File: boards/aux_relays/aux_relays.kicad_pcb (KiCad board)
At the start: 2 copper layers, 82.6 x 40.1 mm, 44 parts, among them J1 Conn_01x15, J2 Conn_01x15, K1 EC2-24NU, K2 EC2-24NU, K3 EC2-24NU, K4 EC2-24NU, K5 EC2-24NU, Q1 MMBT2907, SW1 SW_SPDT, SW2 SW_SPDT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

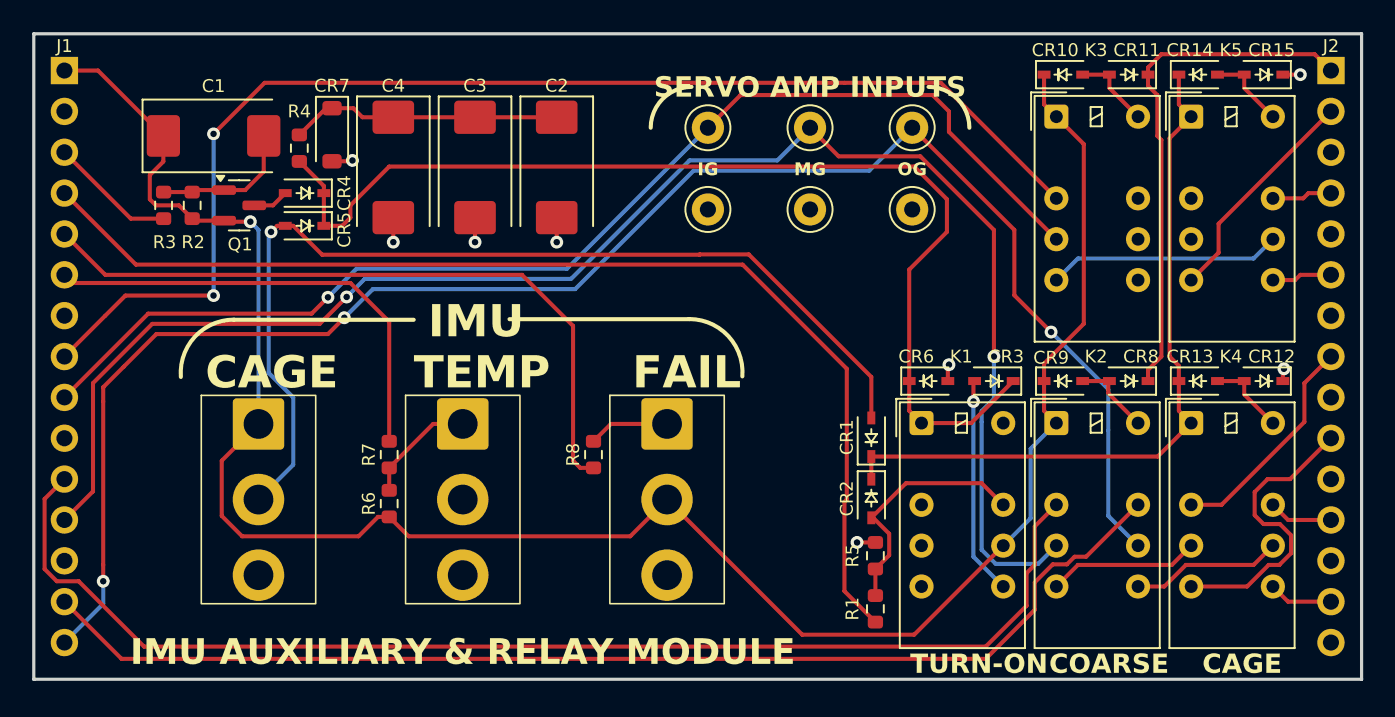
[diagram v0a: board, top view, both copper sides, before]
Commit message: Corrected switch layouts for auxiliary relays and LM switching boards
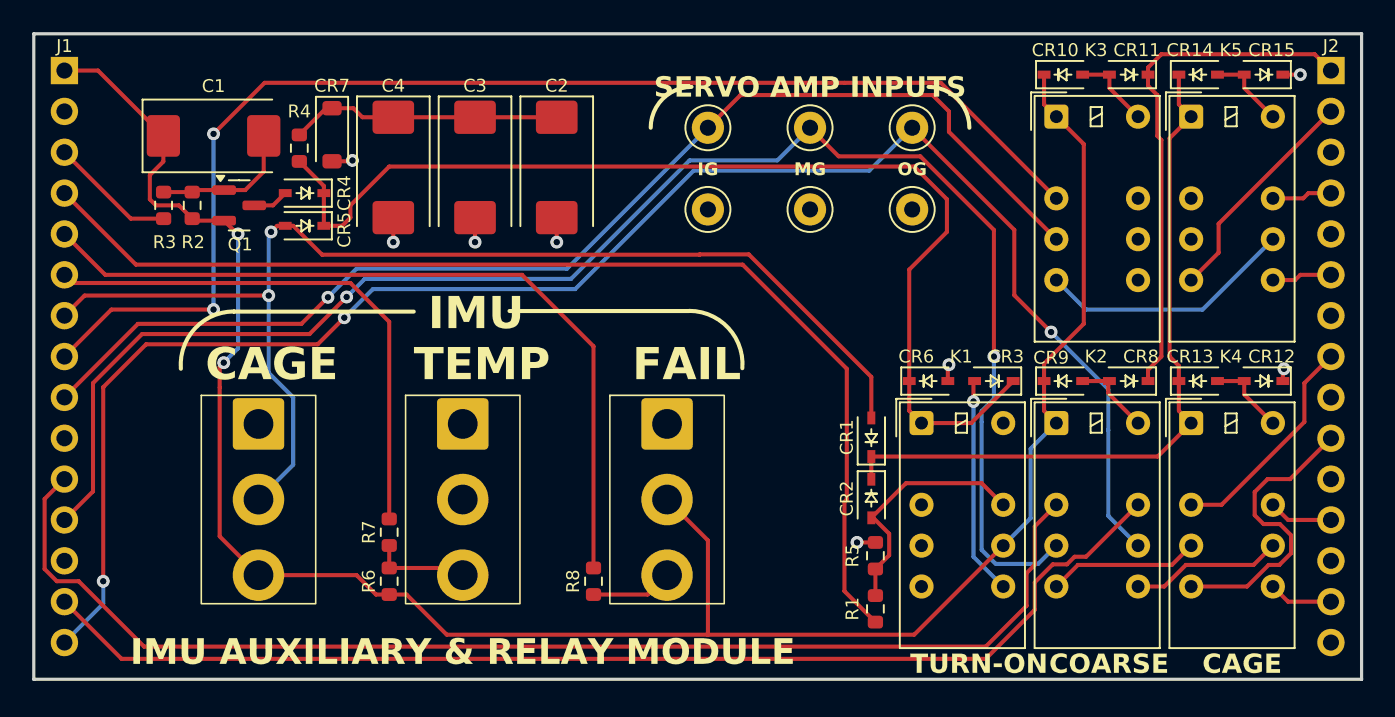
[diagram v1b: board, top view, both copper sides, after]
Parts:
- R6: value 1000 -> 4300
- R7: value 1000 -> 100
- moved R8 7.87 mm to (136.4, 110.2), turned to 90 degrees
- moved R6 4.83 mm to (123.7, 110.2)
- moved R7 4.83 mm to (123.7, 107.2)
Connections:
- CR1 pad 2: Net-(CR1-A) -> /CAGE
- CR5 pad 2: Net-(CR1-A) -> /CAGE
- J1 pad 7: GND -> /CAGE
- J2 pad 2: /CAGE -> /CDU_CAGE
- K5 pad 5: /CAGE -> /CDU_CAGE
- R6 pad 1: Net-(SW2-A) -> Net-(SW2-C)
- R7 pad 1: Net-(SW2-A) -> Net-(SW2-C)
- R8 pad 1: Net-(SW3-A) -> Net-(SW3-C)
- SW1 pad 1: +28V -> unconnected-(SW1-A-Pad1)
- SW1 pad 2: Net-(CR1-A) -> /CAGE
- SW1 pad 3: unconnected-(SW1-C-Pad3) -> +28V
- SW2 pad 1: Net-(SW2-A) -> unconnected-(SW2-A-Pad1)
- SW2 pad 3: unconnected-(SW2-C-Pad3) -> Net-(SW2-C)
- SW3 pad 1: Net-(SW3-A) -> unconnected-(SW3-A-Pad1)
- SW3 pad 3: unconnected-(SW3-C-Pad3) -> Net-(SW3-C)
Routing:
- net Net-(CR1-A): track 62.2 -> 0.00 mm, vias 1 -> 0
- net /CAGE: track 14.1 -> 75.4 mm, vias 0 -> 2
- net /CDU_CAGE: track 0.00 -> 14.1 mm
- net Net-(SW2-A): track 7.10 -> 0.00 mm
- net Net-(SW2-C): track 0.00 -> 6.15 mm
- net +28V: track 128.2 -> 134.2 mm, vias 1 -> 2
- net /IMUFAL: track 43.8 -> 49.6 mm
- net Net-(SW3-C): track 0.00 -> 5.07 mm
- net Net-(SW3-A): track 5.02 -> 0.00 mm
- net /TEMPIN: track 28.8 -> 33.7 mm
- net /IG_CA_CAGE: track 14.5 -> 16.0 mm
- net /IG_ERROR: track 77.8 -> 78.3 mm
